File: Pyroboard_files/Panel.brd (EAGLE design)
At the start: 40 parts, among them IC1 TINY85, IC2 TINY85

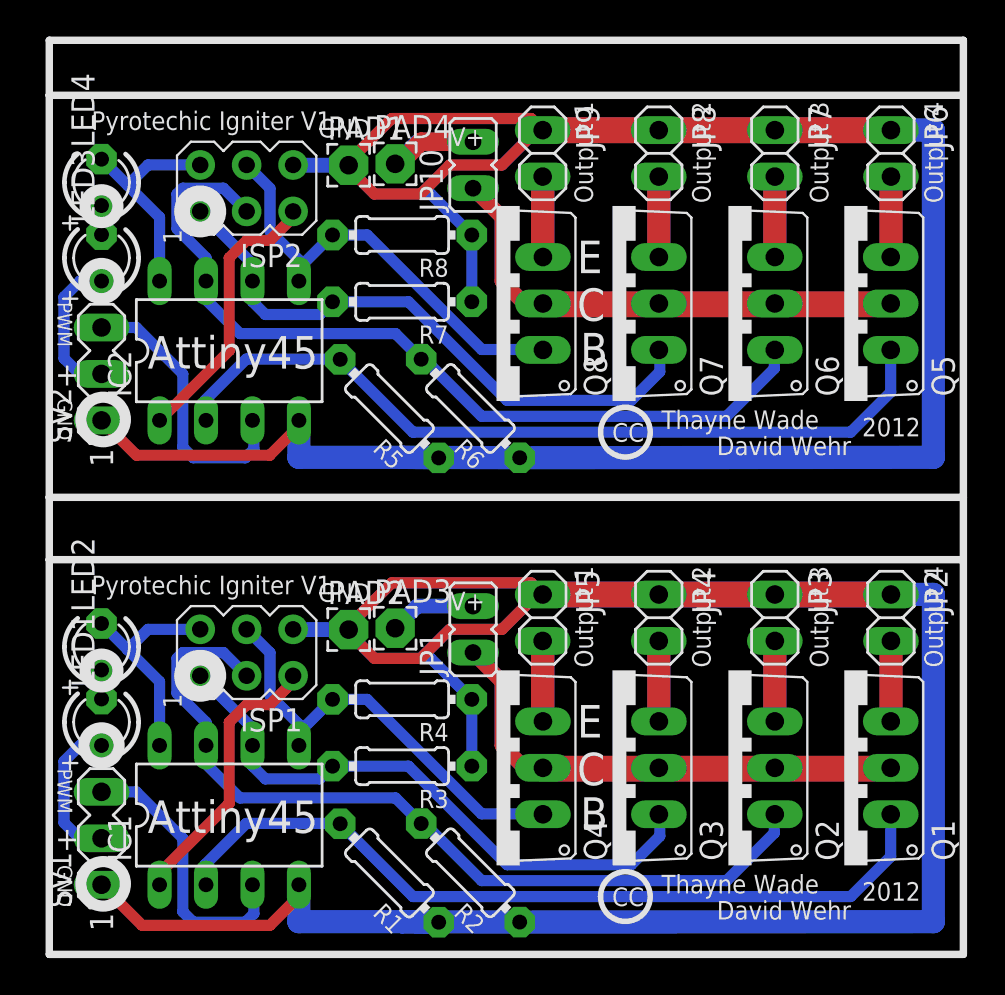
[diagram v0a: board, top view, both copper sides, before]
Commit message: Minor compatibility mod
Threshold info, output pins (Specific to Attiny 45/85 board)
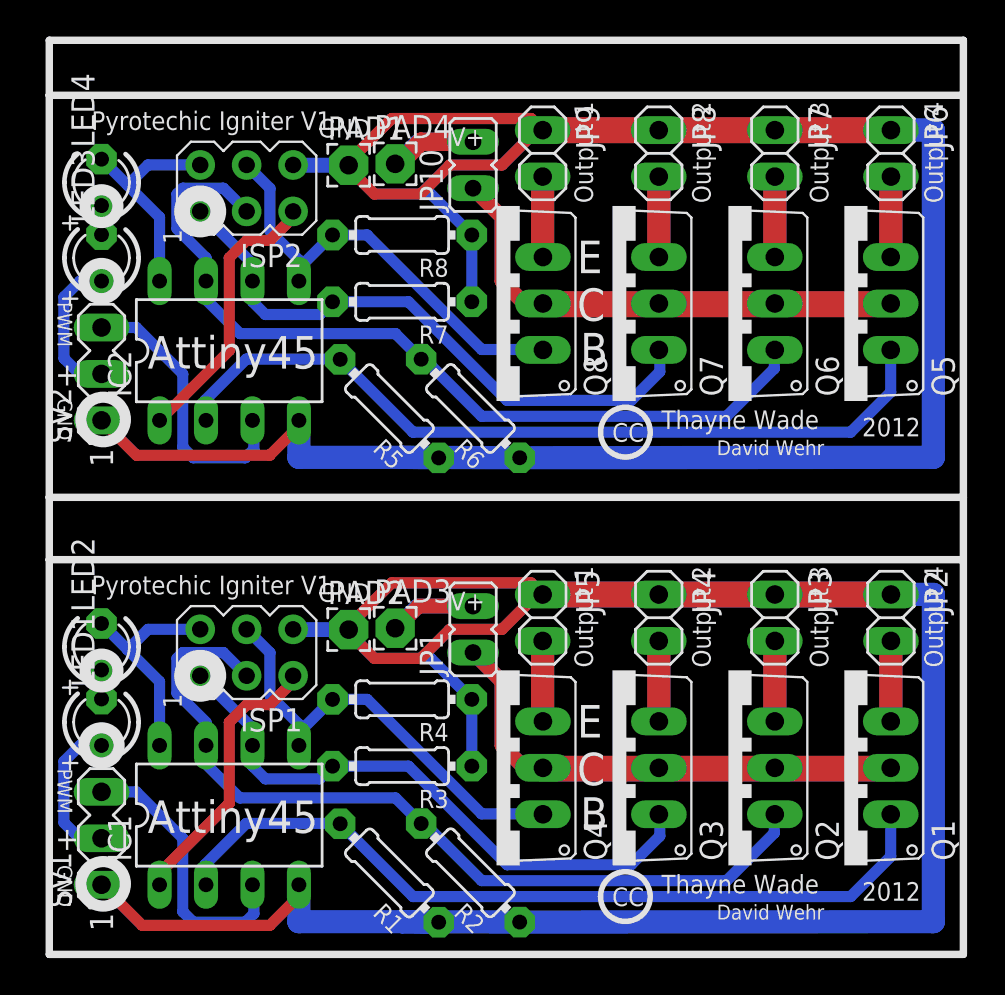
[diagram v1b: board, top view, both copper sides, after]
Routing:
- net S$1: track 0.00 -> 4.84 mm
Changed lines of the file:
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@@
 <text x="0.3175" y="5.715" size="1.27" layer="21">+</text>
 <text x="0.4445" y="4.8895" size="0.8128" layer="21" rot="SR270">GND</text>
-<text x="36.5125" y="1.905" size="1.016" layer="21">David Wehr </text>
+<text x="36.5125" y="1.905" size="0.8128" layer="21">David Wehr </text>
 <text x="2.307040625" y="19.695721875" size="1.016" layer="21">Pyrotechic Igniter V1</text>
 <text x="4.4831" y="5.08" size="1.27" layer="125" ratio="10" rot="R90">IC1</text>
@@
 <text x="0.3175" y="31.115" size="1.27" layer="21">+</text>
 <text x="0.4445" y="30.4165" size="0.8128" layer="21" rot="SR270">GND</text>
-<text x="36.5125" y="27.305" size="1.016" layer="21">David Wehr </text>
+<text x="36.5125" y="27.305" size="0.8128" layer="21">David Wehr </text>
 <text x="2.307040625" y="45.095721875" size="1.016" layer="21">Pyrotechic Igniter V1</text>
 <text x="4.4831" y="30.48" size="1.27" layer="125" ratio="10" rot="R90">IC1</text>
@@
 <wire x1="20.32" y1="44.45" x2="23.1775" y2="44.45" width="1.016" layer="1"/>
 </signal>
+<signal name="S$1">
+<wire x1="18.923" y1="17.78" x2="20.193" y2="19.05" width="0.8128" layer="1"/>
+<wire x1="20.193" y1="19.05" x2="23.241" y2="19.05" width="0.8128" layer="1"/>
+</signal>
 </signals>
